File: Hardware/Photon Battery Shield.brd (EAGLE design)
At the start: 35.6 x 35.6 mm, 23 parts, among them J1 POWER_JACKSMD, U1 MCP73831, U2 MAX1704X

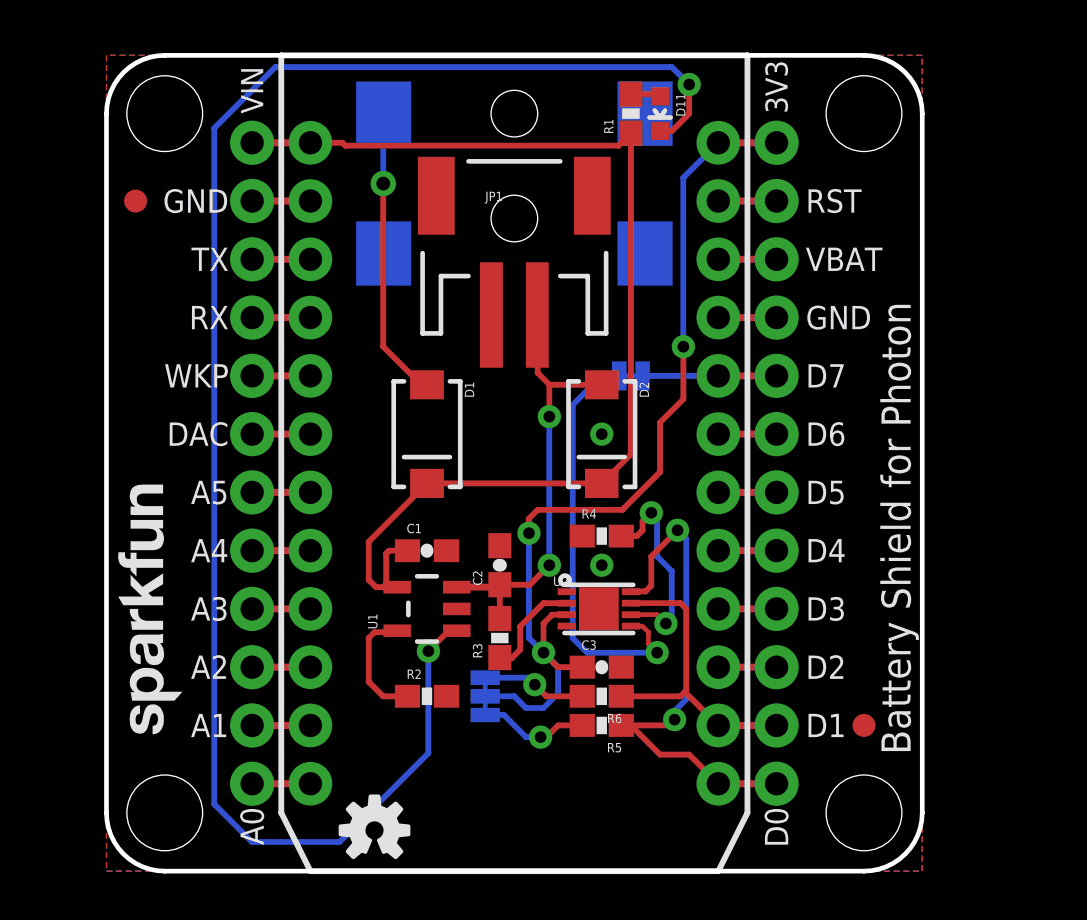
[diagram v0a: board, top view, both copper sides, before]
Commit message: Adjusting VIN route, GND vias. Checklist stuff.
- Adding measures
- Adding PROD_ID to some parts
- Re-routed ALERT pin to D6
- Added MAx17043 i2c address to schematic
- Labeled jumpers ("Pullups" and "Alert")
- Routed traces from fuel gauge directly out of pads. (Added tRestrict to
  make sure GND traces didn't come out sides.)
- Labeled LED "CHG"
- Re-sized "5V" silk
- Changed version number to "v01", added to b copper
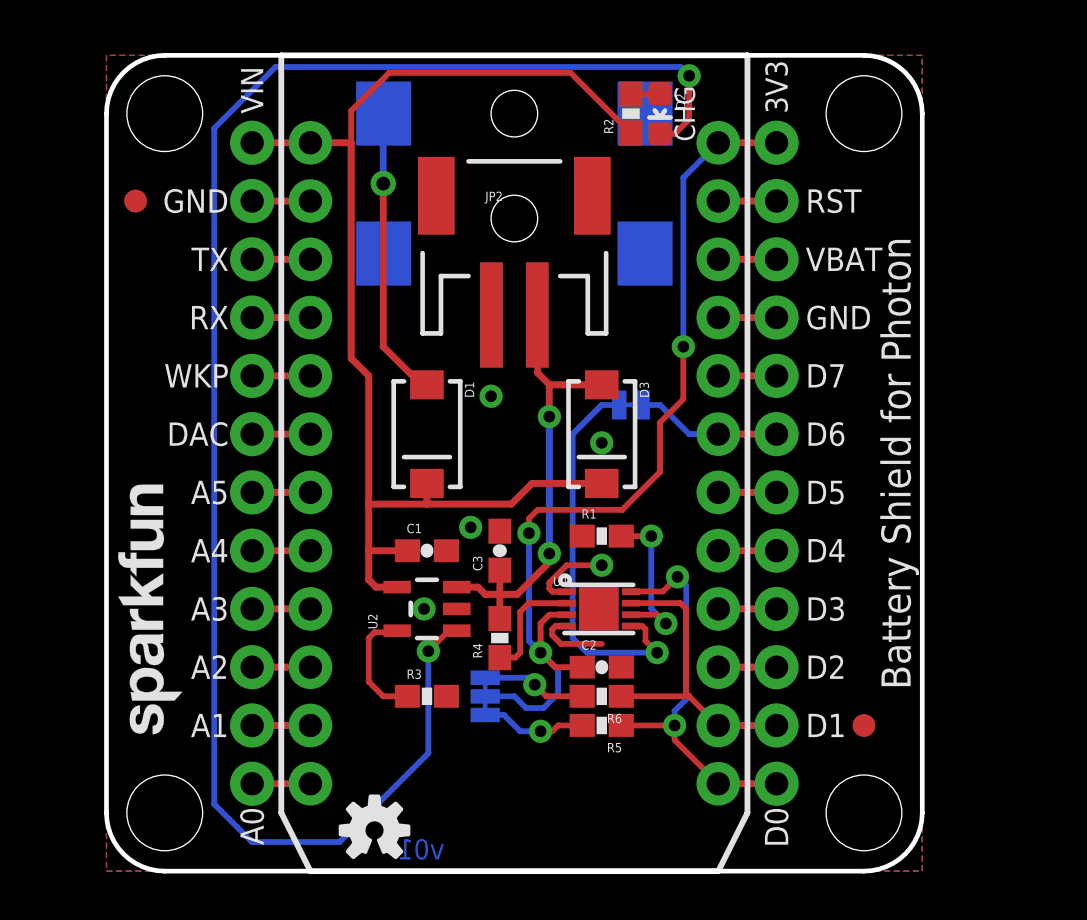
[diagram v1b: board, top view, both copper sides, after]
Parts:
- removed D11: RED, SparkFun-LED:LED-0603
- removed J1: POWER_JACKSMD, SparkFun-Connectors:POWER_JACK_SMD
- added D3: MBRA140, SparkFun-DiscreteSemi:SMA-DIODE
- added FRAME1: (no value), SparkFun-Aesthetics:CREATIVE_COMMONS
- added JP2: (no value), SparkFun-Connectors:JST-2-SMD
- C1: device SparkFun-Passives:0603-CAP -> SparkFun-Capacitors:0603-CAP
- C2: value 4.7uF -> 1.0uF; device SparkFun-Passives:0603-CAP -> SparkFun-Capacitors:0603-CAP
- C3: value (none) -> 4.7uF; device SparkFun-Passives:0603-CAP -> SparkFun-Capacitors:0603-CAP
- D2: value MBRA140 -> RED; device SparkFun-DiscreteSemi:SMA-DIODE -> SparkFun-LED:LED-0603
- JP1: value (none) -> DNP; device SparkFun-Connectors:JST-2-SMD -> SparkFun-Connectors:POWER_JACK_SMD
- LOGO2: value (none) -> OSHW-LOGOS
- R1: value 330 -> 1K; device SparkFun-Passives:0603-RES -> SparkFun-Resistors:0603-RES
- R2: value 2K -> 330; device SparkFun-Passives:0603-RES -> SparkFun-Resistors:0603-RES
- R3: value 1K -> 2.0k; device SparkFun-Passives:0603-RES -> SparkFun-Resistors:0603-RES
- R4: device SparkFun-Passives:0603-RES -> SparkFun-Resistors:0603-RES
- U1: value MCP73831 -> MAX1704X; device SparkFun-PowerIC:SOT23-5 -> SparkFun-PowerIC:TDFN-8
- U2: value MAX1704X -> MCP73831; device SparkFun-PowerIC:TDFN-8 -> SparkFun-PowerIC:SOT23-5
- moved R2 26.9 mm to (22.9, 33.0), turned to 90 degrees
- moved R1 18.5 mm to (21.6, 14.6), turned to 0 degrees
- moved D2 14.2 mm to (24.1, 33.0), turned to 180 degrees
- moved U1 7.49 mm to (21.5, 11.4), turned to 0 degrees
- moved U2 7.49 mm to (14.0, 11.4), turned to 90 degrees
- moved C3 6.75 mm to (17.1, 14.0), turned to 90 degrees
- moved C2 6.29 mm to (21.6, 8.89), turned to 0 degrees
- moved R4 6.29 mm to (17.1, 10.2), turned to 90 degrees
- moved JP1 5.08 mm to (17.8, 33.0), flipped to the bottom, turned to 270 degrees
- moved R3 4.07 mm to (14.0, 7.62), turned to 0 degrees
- moved SJ1 1.27 mm to (22.9, 20.3)
- renumbered U$1 to LOGO2
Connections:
- removed net D7: JP3.20, JP3.D7, SJ1.2
- new net D6: JP3.19, JP3.D6, SJ1.2
- net 3.3V: now also C2.1, U1.3; no longer C3.1, U2.3
- net GND: now also JP1.GND, JP1.P$4, JP2.1, R1.1, R3.2, U1.1, U1.4, U1.EP, U2.2; no longer J1.GND, J1.P$4, JP1.1, R2.2, R4.1, U1.2, U2.1, U2.4, U2.EP
- net N$1: now also D2.A, R2.2; no longer D11.A, R1.2
- net N$2: now also D2.C, U2.1; no longer D11.C, U1.1
- net N$3: now also R3.1, U2.5; no longer R2.1, U1.5
- net N$4: now also U1.5; no longer U2.5
- net N$5: now also R4.1, U1.2; no longer R3.1, U2.2
- net N$6: now also R1.2, U1.6; no longer R4.2, U2.6
- net N$8: now also JP1.VIN0; no longer J1.VIN0
- net SCL: now also U1.7; no longer U2.7
- net SDA: now also U1.8; no longer U2.8
- net VBAT: now also C3.1, D3.A, JP2.2, R4.2, U2.3; no longer C2.1, D2.A, JP1.2, R3.2, U1.3
- net VIN: now also D3.C, R2.1, U2.4; no longer D2.C, R1.1, U1.4
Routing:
- net GND: track 0.00 -> 6.93 mm, vias 2 -> 5
- net SDA: track 20.2 -> 15.2 mm
- net VIN: track 46.8 -> 51.0 mm
- net D6: track 0.00 -> 3.83 mm
- net D7: track 3.30 -> 0.00 mm
- net N$6: track 8.93 -> 7.06 mm
- net N$4: track 18.6 -> 17.3 mm
- net VBAT: track 19.3 -> 20.1 mm
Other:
- board text added: "Alert"
- board text added: "CHG"
- board text added: "Cody Knutson"
- board text added: "Pull-ups"
- board text added: "v01"

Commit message: Checklist Fixes
(1) Added input voltage label on SCH

(2) Added description for SJ1 in SCH

(3) Added description for SJ2 in SCH

(4) Fixed traces on R2, D1, and STAT pad on MCP

(5) 3-way pull up now has SDA and SCL BPlace objects added next to the
jumper

(6) Resized Board Name text objects to prevent overlap with VBAT text
object

(7) "CHG" TPlace text, and the "Pull-ups" and "ALERT" BPlace text
objects have been changed to Vector font type.
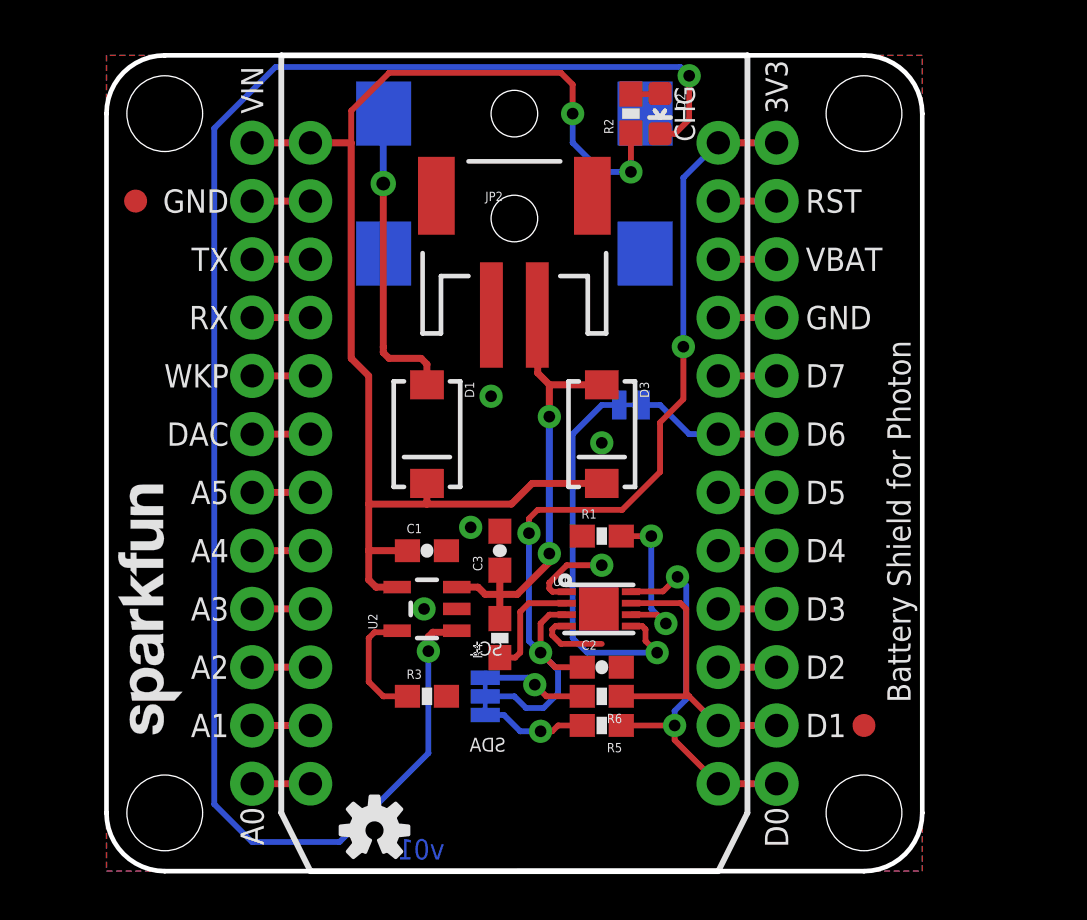
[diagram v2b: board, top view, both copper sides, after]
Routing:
- net VIN: track 51.0 -> 54.9 mm, vias 0 -> 2
- net N$8: track 12.8 -> 13.7 mm
- net N$2: track 72.5 -> 73.3 mm
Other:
- board text added: "SCL"
- board text added: "SDA"
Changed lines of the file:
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@@
 <?xml version="1.0" encoding="utf-8"?>
 <!DOCTYPE eagle SYSTEM "eagle.dtd">
-<eagle version="7.1.0">
+<eagle version="7.2.0">
 <drawing>
 <settings>
@@
 <layer number="47" name="Measures" color="7" fill="1" visible="no" active="yes"/>
 <layer number="48" name="Document" color="7" fill="1" visible="no" active="yes"/>
-<layer number="49" name="Reference" color="7" fill="1" visible="yes" active="yes"/>
+<layer number="49" name="Reference" color="7" fill="1" visible="no" active="yes"/>
 <layer number="50" name="dxf" color="7" fill="1" visible="no" active="no"/>
 <layer number="51" name="tDocu" color="6" fill="1" visible="yes" active="yes"/>
@@
 <wire x1="0" y1="2.54" x2="0" y2="33.02" width="0.2032" layer="20"/>
 <wire x1="0" y1="33.02" x2="2.54" y2="35.56" width="0.2032" layer="20" curve="-90"/>
-<text x="35.052" y="17.78" size="1.27" layer="21" font="vector" ratio="15" rot="R90" align="bottom-center">Battery Shield for Photon</text>
-<text x="33.782" y="17.78" size="1.27" layer="22" font="vector" ratio="15" rot="MR90" align="bottom-center">Battery Shield for Photon</text>
+<text x="35.052" y="15.24" size="1.016" layer="21" font="vector" ratio="15" rot="R90" align="bottom-center">Battery Shield for Photon</text>
+<text x="34.163" y="15.24" size="1.016" layer="22" font="vector" ratio="15" rot="MR90" align="bottom-center">Battery Shield for Photon</text>
 <text x="17.78" y="21.59" size="1.27" layer="22" font="vector" ratio="15" rot="MR0" align="bottom-center">5V</text>
 <wire x1="19.812" y1="12.4714" x2="20.193" y2="12.4714" width="0.254" layer="41"/>
 <wire x1="20.32" y1="10.3886" x2="19.939" y2="10.3886" width="0.254" layer="41"/>
-<text x="15.24" y="7.62" size="0.8128" layer="22" ratio="15" rot="MR270" align="bottom-center">Pull-ups</text>
-<text x="22.86" y="21.59" size="0.8128" layer="22" ratio="15" rot="MR0" align="bottom-center">Alert</text>
-<text x="24.765" y="33.02" size="0.889" layer="21" ratio="15" rot="R270" align="bottom-center">CHG</text>
+<text x="15.24" y="7.62" size="0.762" layer="22" font="vector" ratio="15" rot="MR270" align="bottom-center">Pull-ups</text>
+<text x="22.86" y="21.59" size="0.8128" layer="22" font="vector" ratio="15" rot="MR0" align="bottom-center">Alert</text>
+<text x="24.765" y="33.02" size="0.889" layer="21" font="vector" ratio="15" rot="R270" align="bottom-center">CHG</text>
 <text x="13.716" y="0.508" size="0.889" layer="16" font="vector" ratio="15" rot="MR0" align="bottom-center">v01</text>
 <text x="21.59" y="-15.24" size="1.27" layer="51" ratio="15">Cody Knutson</text>
@@
 <dimension x1="2.54" y1="33.02" x2="2.54" y2="0" x3="-3.81" y3="16.51" textsize="0.889" textratio="15" layer="47" dtype="horizontal" width="0.127" unit="inch"/>
 <dimension x1="2.54" y1="35.56" x2="2.54" y2="0" x3="-6.35" y3="17.78" textsize="0.889" textratio="15" layer="47" dtype="horizontal" width="0.127" unit="inch"/>
+<text x="17.399" y="5.207" size="0.6096" layer="21" font="vector" ratio="15" rot="MR0">SDA</text>
+<text x="17.272" y="9.398" size="0.6096" layer="21" font="vector" ratio="15" rot="MR0">SCL</text>
 </plain>
 <attributes>
@@
 <wire x1="21.59" y1="16.9" x2="18.551" y2="16.9" width="0.3048" layer="1"/>
 <wire x1="13.97" y1="16.002" x2="11.43" y2="16.002" width="0.3048" layer="1"/>
-<wire x1="22.86" y1="32.17" x2="20.232" y2="34.798" width="0.254" layer="1"/>
-<wire x1="20.232" y1="34.798" x2="12.319" y2="34.798" width="0.254" layer="1"/>
 <wire x1="12.319" y1="34.798" x2="10.668" y2="33.147" width="0.254" layer="1"/>
 <wire x1="10.668" y1="33.147" x2="10.668" y2="31.75" width="0.254" layer="1"/>
+<wire x1="22.86" y1="32.17" x2="22.86" y2="30.48" width="0.254" layer="1"/>
+<via x="22.86" y="30.48" extent="1-16" drill="0.508"/>
+<wire x1="22.86" y1="30.48" x2="21.59" y2="30.48" width="0.254" layer="16"/>
+<wire x1="21.59" y1="30.48" x2="20.32" y2="31.75" width="0.254" layer="16"/>
+<wire x1="20.32" y1="31.75" x2="20.32" y2="33.02" width="0.254" layer="16"/>
+<wire x1="20.32" y1="33.02" x2="20.232" y2="34.798" width="0" layer="19" extent="1-16"/>
+<wire x1="12.319" y1="34.798" x2="19.812" y2="34.798" width="0.254" layer="1"/>
+<wire x1="19.812" y1="34.798" x2="20.32" y2="34.29" width="0.254" layer="1"/>
+<via x="20.32" y="33.02" extent="1-16" drill="0.508"/>
+<wire x1="20.32" y1="33.02" x2="20.32" y2="34.29" width="0.254" layer="1"/>
 </signal>
 <signal name="N$1">
@@
 <wire x1="25.4" y1="34.671" x2="25.4" y2="32.766" width="0.254" layer="1"/>
 <wire x1="15.2701" y1="10.48" x2="14.92" y2="10.48" width="0.254" layer="1"/>
-<wire x1="14.92" y1="10.48" x2="14.031" y2="9.591" width="0.254" layer="1"/>
 <wire x1="24.13" y1="32.143" x2="24.777" y2="32.143" width="0.254" layer="1"/>
 <wire x1="25.4" y1="32.766" x2="24.777" y2="32.143" width="0.254" layer="1"/>
+<wire x1="14.031" y1="9.591" x2="14.031" y2="10.221" width="0.3048" layer="1"/>
+<wire x1="14.031" y1="10.221" x2="14.224" y2="10.414" width="0.3048" layer="1"/>
+<wire x1="14.224" y1="10.414" x2="15.2041" y2="10.414" width="0.3048" layer="1"/>
+<wire x1="15.2041" y1="10.414" x2="15.2701" y2="10.48" width="0.3048" layer="1"/>
 </signal>
 <signal name="N$3">
@@
 <contactref element="D1" pad="A"/>
 <wire x1="13.97" y1="21.2" x2="13.725" y2="21.2" width="0.3048" layer="1"/>
-<wire x1="13.725" y1="21.2" x2="12.065" y2="22.86" width="0.3048" layer="1"/>
 <wire x1="12.065" y1="22.86" x2="12.065" y2="29.972" width="0.3048" layer="1"/>
 <via x="12.065" y="29.972" extent="1-16" drill="0.6"/>
 <wire x1="12.065" y1="29.972" x2="12.065" y2="33.005" width="0.3048" layer="16"/>
 <wire x1="12.065" y1="33.005" x2="12.08" y2="33.02" width="0.254" layer="16"/>
+<wire x1="12.065" y1="22.86" x2="12.065" y2="22.606" width="0.3048" layer="1"/>
+<wire x1="12.065" y1="22.606" x2="12.319" y2="22.352" width="0.3048" layer="1"/>
+<wire x1="12.319" y1="22.352" x2="13.716" y2="22.352" width="0.3048" layer="1"/>
+<wire x1="13.716" y1="22.352" x2="13.97" y2="22.098" width="0.3048" layer="1"/>
+<wire x1="13.97" y1="22.098" x2="13.97" y2="21.2" width="0.3048" layer="1"/>
 </signal>
 <signal name="N$7">

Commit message: Connecting GND - Photon pin 21 - to the GND plane.
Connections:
- net GND: now also JP3.21, JP3.GND@2
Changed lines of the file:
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@@
 <?xml version="1.0" encoding="utf-8"?>
 <!DOCTYPE eagle SYSTEM "eagle.dtd">
-<eagle version="7.2.0">
+<eagle version="7.1.0">
 <drawing>
 <settings>
@@
 <wire x1="19.812" y1="9.906" x2="21.59" y2="9.906" width="0.254" layer="1"/>
 <contactref element="JP2" pad="1"/>
+<contactref element="JP3" pad="GND@2"/>
+<contactref element="JP3" pad="21"/>
 </signal>
 <signal name="VIN">
@@
 <wire x1="21.59" y1="30.48" x2="20.32" y2="31.75" width="0.254" layer="16"/>
 <wire x1="20.32" y1="31.75" x2="20.32" y2="33.02" width="0.254" layer="16"/>
-<wire x1="20.32" y1="33.02" x2="20.232" y2="34.798" width="0" layer="19" extent="1-16"/>
 <wire x1="12.319" y1="34.798" x2="19.812" y2="34.798" width="0.254" layer="1"/>
 <wire x1="19.812" y1="34.798" x2="20.32" y2="34.29" width="0.254" layer="1"/>

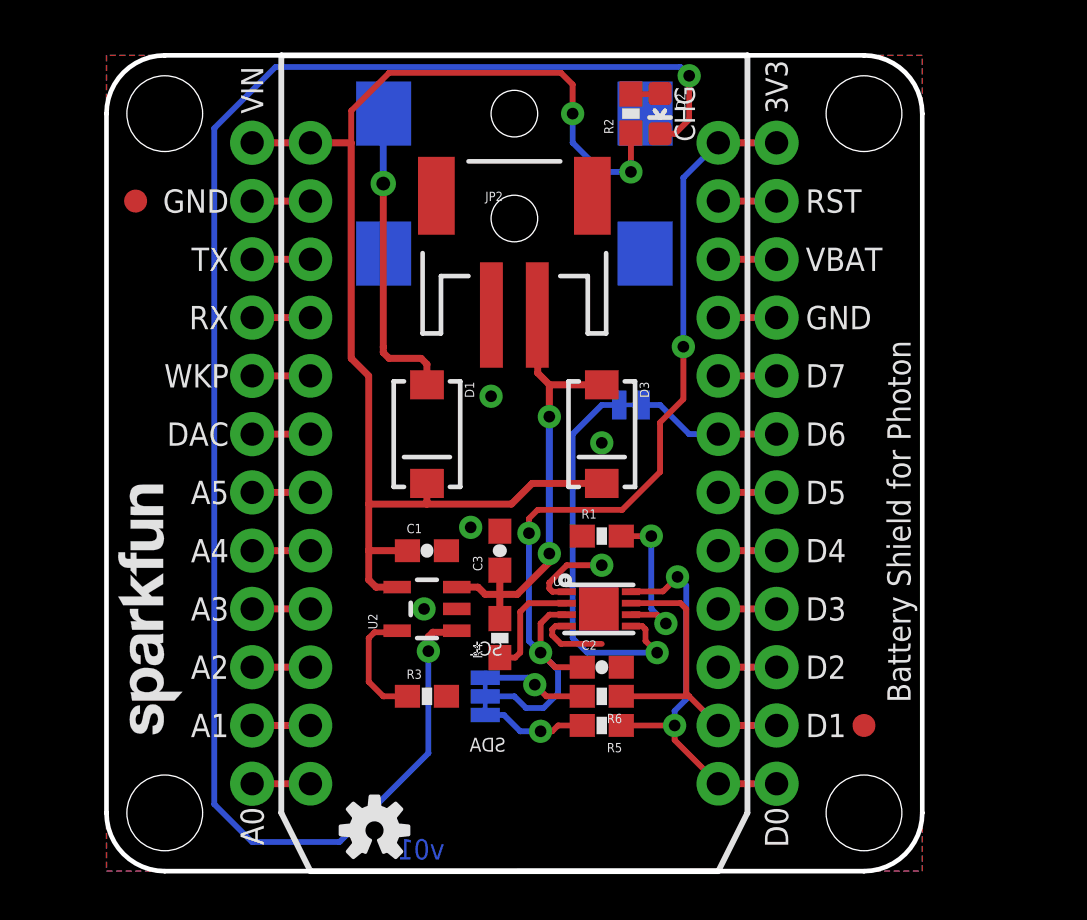
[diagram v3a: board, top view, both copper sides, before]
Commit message: Updating Photon package to WIDE footprint. Defaulting SJ1 to open.
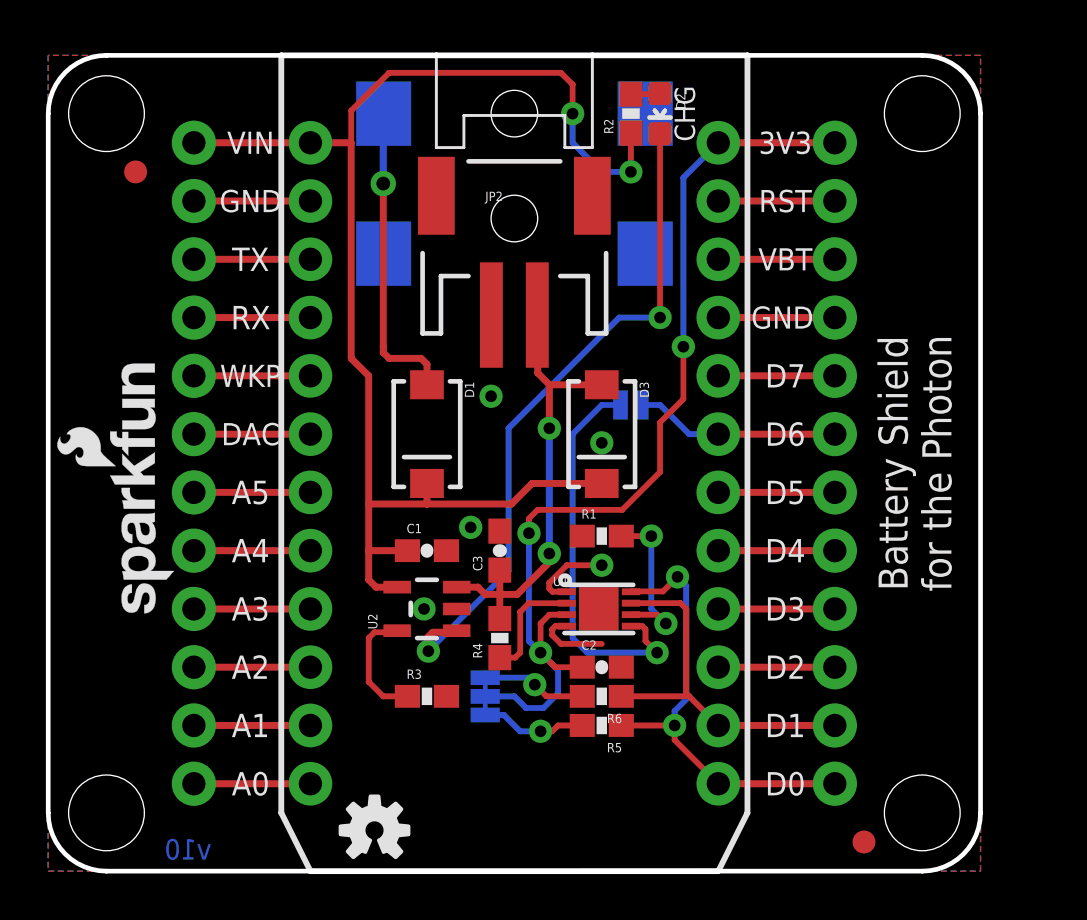
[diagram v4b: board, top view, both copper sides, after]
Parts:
- removed LOGO1: SFE_LOGO_NAME.1_INCH, SparkFun-Aesthetics:SFE_LOGO_NAME_.1
- added LOGO3: SFE_LOGO_NAME_FLAME.1_INCH, SparkFun-Aesthetics:SFE_LOGO_NAME_FLAME_.1
- JP3: value SPARK_PHOTONTEMPLATE -> SPARK_PHOTONTEMPLATE_WIDE; device template_temp:SPARK_PHOTON_TEMPLATE -> template_temp:SPARK_PHOTON_TEMPLATE_WIDE
- SJ1: value SOLDERJUMPERTRACE -> alert; device SparkFun-Passives:SJ_2S-TRACE -> SparkFun-Passives:PAD-JUMPER-2-NO_YES_SILK
- moved FID1 5.08 mm to (33.0, 1.27)
- moved FID2 1.27 mm to (1.27, 30.5)
- turned SJ1 to 0 degrees
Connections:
- net D6: now also SJ1.1; no longer SJ1.2
- net N$4: now also SJ1.2; no longer SJ1.1
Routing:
- net N$2: track 73.3 -> 30.1 mm
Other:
- board size 35.6 x 35.6 mm -> 40.6 x 35.6 mm
- board text added: "Battery Shield for the Photon"
- board text added: "v10"
- board text removed: "Battery Shield for Photon"
- board text removed: "v01"
